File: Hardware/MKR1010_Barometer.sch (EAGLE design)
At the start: 2 parts

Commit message: schematic capture
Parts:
- removed U$1: ARDUINOMICRO, adafruit:ARDUINOMICRO
- added D1: 1N4001, SparkFun-DiscreteSemi:DIODE-PTH
- added J1: (no value), con-jack:JACK-PLUG0
- added J2, J3: 1X2-3.5MM, adafruit:1X2-3.5MM
- added M1: MOTOR10MM, SparkFun-Electromechanical:MOTOR10MM
- added MKR1010: ARDUINOMICRO, adafruit:ARDUINOMICRO
- added T1: TIP122, transistor:TIP122
- R1: value (none) -> 220
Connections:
- new net GND: D1.A, J1.1, J3.1, T1.E
- new net N$2: R1.1, T1.B
- new net N$3: D1.C, M1.-, T1.C
- new net N$4: J1.3, J2.2, M1.+, MKR1010.5V
- new net N$5: J2.1, MKR1010.6
- net N$1: now also MKR1010.7; no longer U$1.NC@2
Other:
- note added: "MKR1010"
- moved on the sheet: R1

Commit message: added terminal to attach MPL115A2
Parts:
- added J4, J5: 1X2-3.5MM, adafruit:1X2-3.5MM
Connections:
- new net N$6: J4.1, MKR1010.SCK
- new net N$7: J4.2, MKR1010.MISO
- net GND: now also J5.2
- net N$4: now also J5.1
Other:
- note added: "Data In Vcc"
- note added: "GND"
- note added: "SCL SDA"
- note added: "To LED Matrix"
- note added: "To MPL115A2 Sensor"
- note added: "Vcc GND"
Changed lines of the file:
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@@
 <part name="SUPPLY2" library="supply2" library_urn="urn:adsk.eagle:library:372" deviceset="GND" device=""/>
 <part name="SUPPLY3" library="supply2" library_urn="urn:adsk.eagle:library:372" deviceset="GND" device=""/>
+<part name="J4" library="adafruit" library_urn="urn:adsk.eagle:library:420" deviceset="1X2" device="-3.5MM" package3d_urn="urn:adsk.eagle:package:6240635/1"/>
+<part name="J5" library="adafruit" library_urn="urn:adsk.eagle:library:420" deviceset="1X2" device="-3.5MM" package3d_urn="urn:adsk.eagle:package:6240635/1"/>
+<part name="SUPPLY4" library="supply2" library_urn="urn:adsk.eagle:library:372" deviceset="GND" device=""/>
 </parts>
 <sheets>
@@
 <plain>
 <text x="0" y="58.42" size="1.778" layer="94" rot="R90">MKR1010</text>
+<text x="43.18" y="45.72" size="1.778" layer="91">To LED Matrix</text>
+<text x="43.18" y="12.7" size="1.778" layer="91">To MPL115A2 Sensor</text>
+<text x="45.72" y="38.1" size="1.778" layer="91">Data In
+Vcc</text>
+<text x="45.72" y="30.48" size="1.778" layer="91">GND</text>
+<text x="45.72" y="5.08" size="1.778" layer="91">SCL
+SDA</text>
+<text x="45.72" y="-5.08" size="1.778" layer="91">Vcc
+GND</text>
 </plain>
 <instances>
@@
 <instance part="SUPPLY3" gate="GND" x="30.48" y="20.32" smashed="yes">
 <attribute name="VALUE" x="28.575" y="17.145" size="1.778" layer="96"/>
+</instance>
+<instance part="J4" gate="G$1" x="38.1" y="5.08" smashed="yes"/>
+<instance part="J5" gate="G$1" x="38.1" y="-5.08" smashed="yes"/>
+<instance part="SUPPLY4" gate="GND" x="30.48" y="-10.16" smashed="yes">
+<attribute name="VALUE" x="28.575" y="-13.335" size="1.778" layer="96"/>
 </instance>
 </instances>
@@
 <wire x1="-22.86" y1="91.44" x2="-22.86" y2="88.9" width="0.1524" layer="91"/>
 </segment>
+<segment>
+<pinref part="J5" gate="G$1" pin="2"/>
+<wire x1="33.02" y1="-5.08" x2="30.48" y2="-5.08" width="0.1524" layer="91"/>
+<pinref part="SUPPLY4" gate="GND" pin="GND"/>
+<wire x1="30.48" y1="-5.08" x2="30.48" y2="-7.62" width="0.1524" layer="91"/>
+</segment>
 </net>
 <net name="N$5" class="0">
@@
 <pinref part="J2" gate="G$1" pin="2"/>
 <wire x1="15.24" y1="38.1" x2="33.02" y2="38.1" width="0.1524" layer="91"/>
+<pinref part="J5" gate="G$1" pin="1"/>
+<wire x1="33.02" y1="-2.54" x2="-17.78" y2="-2.54" width="0.1524" layer="91"/>
+<wire x1="-17.78" y1="-2.54" x2="-17.78" y2="30.48" width="0.1524" layer="91"/>
+<junction x="-17.78" y="30.48"/>
+</segment>
+</net>
+<net name="N$6" class="0">
+<segment>
+<pinref part="MKR1010" gate="G$1" pin="SCK"/>
+<pinref part="J4" gate="G$1" pin="1"/>
+<wire x1="-12.7" y1="38.1" x2="-12.7" y2="7.62" width="0.1524" layer="91"/>
+<wire x1="-12.7" y1="7.62" x2="33.02" y2="7.62" width="0.1524" layer="91"/>
+</segment>
+</net>
+<net name="N$7" class="0">
+<segment>
+<pinref part="MKR1010" gate="G$1" pin="MISO"/>
+<wire x1="-12.7" y1="40.64" x2="-15.24" y2="40.64" width="0.1524" layer="91"/>
+<wire x1="-15.24" y1="40.64" x2="-15.24" y2="5.08" width="0.1524" layer="91"/>
+<pinref part="J4" gate="G$1" pin="2"/>
+<wire x1="-15.24" y1="5.08" x2="33.02" y2="5.08" width="0.1524" layer="91"/>
 </segment>
 </net>
@@
 </drawing>
 <compatibility>
+<note version="6.3" minversion="6.2.2" severity="warning">
+Since Version 6.2.2 text objects can contain more than one line,
+which will not be processed correctly with this version.
+</note>
 <note version="8.2" severity="warning">
 Since Version 8.2, EAGLE supports online libraries. The ids

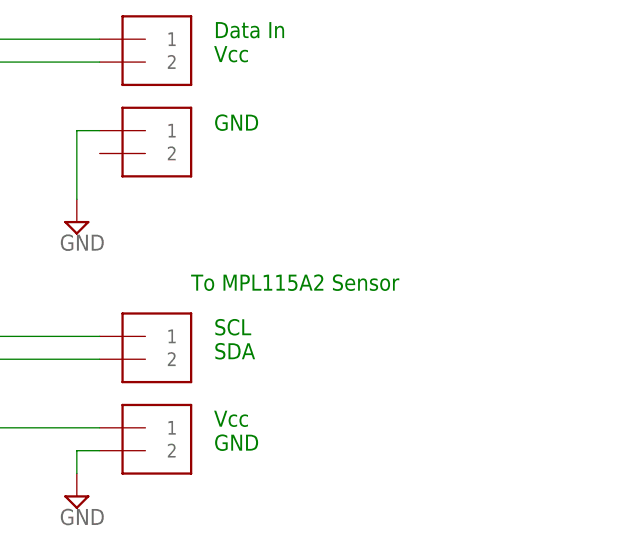
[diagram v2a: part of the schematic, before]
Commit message: Updated schematic with BMP280
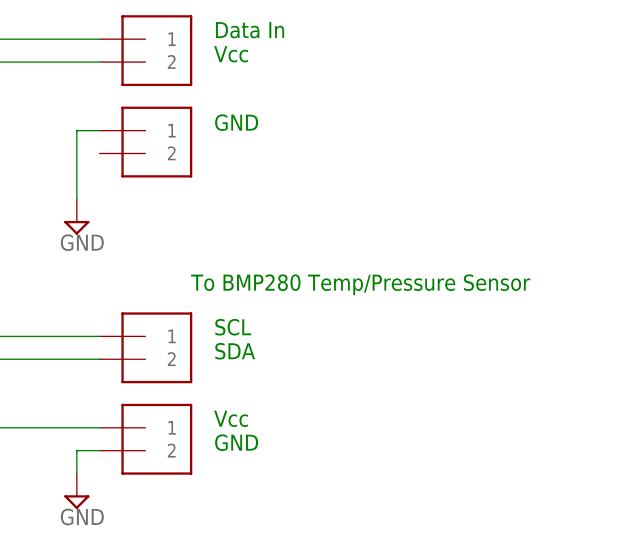
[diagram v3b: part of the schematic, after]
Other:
- note added: "To BMP280 Temp/Pressure Sensor"
- note removed: "To MPL115A2 Sensor"
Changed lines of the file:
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@@
 <grid distance="0.1" unitdist="inch" unit="inch" style="lines" multiple="1" display="no" altdistance="0.01" altunitdist="inch" altunit="inch"/>
 <layers>
-<layer number="1" name="Top" color="4" fill="1" visible="yes" active="no"/>
-<layer number="2" name="Route2" color="16" fill="1" visible="yes" active="no"/>
-<layer number="15" name="Route15" color="23" fill="1" visible="yes" active="no"/>
-<layer number="16" name="Bottom" color="1" fill="1" visible="yes" active="no"/>
-<layer number="17" name="Pads" color="2" fill="1" visible="yes" active="no"/>
-<layer number="18" name="Vias" color="2" fill="1" visible="yes" active="no"/>
-<layer number="19" name="Unrouted" color="6" fill="1" visible="yes" active="no"/>
-<layer number="20" name="Dimension" color="24" fill="1" visible="yes" active="no"/>
-<layer number="21" name="tPlace" color="7" fill="1" visible="yes" active="no"/>
-<layer number="22" name="bPlace" color="7" fill="1" visible="yes" active="no"/>
-<layer number="23" name="tOrigins" color="15" fill="1" visible="yes" active="no"/>
-<layer number="24" name="bOrigins" color="15" fill="1" visible="yes" active="no"/>
-<layer number="25" name="tNames" color="7" fill="1" visible="yes" active="no"/>
-<layer number="26" name="bNames" color="7" fill="1" visible="yes" active="no"/>
-<layer number="27" name="tValues" color="7" fill="1" visible="yes" active="no"/>
-<layer number="28" name="bValues" color="7" fill="1" visible="yes" active="no"/>
+<layer number="1" name="Top" color="4" fill="1" visible="no" active="no"/>
+<layer number="2" name="Route2" color="16" fill="1" visible="no" active="no"/>
+<layer number="15" name="Route15" color="23" fill="1" visible="no" active="no"/>
+<layer number="16" name="Bottom" color="1" fill="1" visible="no" active="no"/>
+<layer number="17" name="Pads" color="2" fill="1" visible="no" active="no"/>
+<layer number="18" name="Vias" color="2" fill="1" visible="no" active="no"/>
+<layer number="19" name="Unrouted" color="6" fill="1" visible="no" active="no"/>
+<layer number="20" name="Dimension" color="24" fill="1" visible="no" active="no"/>
+<layer number="21" name="tPlace" color="7" fill="1" visible="no" active="no"/>
+<layer number="22" name="bPlace" color="7" fill="1" visible="no" active="no"/>
+<layer number="23" name="tOrigins" color="15" fill="1" visible="no" active="no"/>
+<layer number="24" name="bOrigins" color="15" fill="1" visible="no" active="no"/>
+<layer number="25" name="tNames" color="7" fill="1" visible="no" active="no"/>
+<layer number="26" name="bNames" color="7" fill="1" visible="no" active="no"/>
+<layer number="27" name="tValues" color="7" fill="1" visible="no" active="no"/>
+<layer number="28" name="bValues" color="7" fill="1" visible="no" active="no"/>
 <layer number="29" name="tStop" color="7" fill="3" visible="no" active="no"/>
 <layer number="30" name="bStop" color="7" fill="6" visible="no" active="no"/>
@@
 <layer number="35" name="tGlue" color="7" fill="4" visible="no" active="no"/>
 <layer number="36" name="bGlue" color="7" fill="5" visible="no" active="no"/>
-<layer number="37" name="tTest" color="7" fill="1" visible="yes" active="no"/>
-<layer number="38" name="bTest" color="7" fill="1" visible="yes" active="no"/>
+<layer number="37" name="tTest" color="7" fill="1" visible="no" active="no"/>
+<layer number="38" name="bTest" color="7" fill="1" visible="no" active="no"/>
 <layer number="39" name="tKeepout" color="4" fill="11" visible="no" active="no"/>
 <layer number="40" name="bKeepout" color="1" fill="11" visible="no" active="no"/>
@@
 <layer number="44" name="Drills" color="7" fill="1" visible="no" active="no"/>
 <layer number="45" name="Holes" color="7" fill="1" visible="no" active="no"/>
-<layer number="46" name="Milling" color="3" fill="1" visible="yes" active="no"/>
-<layer number="47" name="Measures" color="7" fill="1" visible="yes" active="no"/>
-<layer number="48" name="Document" color="7" fill="1" visible="yes" active="no"/>
-<layer number="49" name="Reference" color="7" fill="1" visible="yes" active="no"/>
-<layer number="50" name="dxf" color="7" fill="1" visible="yes" active="no"/>
-<layer number="51" name="tDocu" color="7" fill="1" visible="yes" active="no"/>
-<layer number="52" name="bDocu" color="7" fill="1" visible="yes" active="no"/>
-<layer number="53" name="tGND_GNDA" color="7" fill="9" visible="yes" active="no"/>
-<layer number="54" name="bGND_GNDA" color="1" fill="9" visible="yes" active="no"/>
-<layer number="56" name="wert" color="7" fill="1" visible="yes" active="no"/>
-<layer number="57" name="tCAD" color="7" fill="1" visible="yes" active="no"/>
-<layer number="59" name="tCarbon" color="7" fill="1" visible="yes" active="no"/>
-<layer number="60" name="bCarbon" color="7" fill="1" visible="yes" active="no"/>
+<layer number="46" name="Milling" color="3" fill="1" visible="no" active="no"/>
+<layer number="47" name="Measures" color="7" fill="1" visible="no" active="no"/>
+<layer number="48" name="Document" color="7" fill="1" visible="no" active="no"/>
+<layer number="49" name="Reference" color="7" fill="1" visible="no" active="no"/>
+<layer number="50" name="dxf" color="7" fill="1" visible="no" active="no"/>
+<layer number="51" name="tDocu" color="7" fill="1" visible="no" active="no"/>
+<layer number="52" name="bDocu" color="7" fill="1" visible="no" active="no"/>
+<layer number="53" name="tGND_GNDA" color="7" fill="9" visible="no" active="no"/>
+<layer number="54" name="bGND_GNDA" color="1" fill="9" visible="no" active="no"/>
+<layer number="56" name="wert" color="7" fill="1" visible="no" active="no"/>
+<layer number="57" name="tCAD" color="7" fill="1" visible="no" active="no"/>
+<layer number="59" name="tCarbon" color="7" fill="1" visible="no" active="no"/>
+<layer number="60" name="bCarbon" color="7" fill="1" visible="no" active="no"/>
 <layer number="88" name="SimResults" color="9" fill="1" visible="yes" active="yes"/>
 <layer number="89" name="SimProbes" color="9" fill="1" visible="yes" active="yes"/>
@@
 <text x="0" y="58.42" size="1.778" layer="94" rot="R90">MKR1010</text>
 <text x="43.18" y="45.72" size="1.778" layer="91">To LED Matrix</text>
-<text x="43.18" y="12.7" size="1.778" layer="91">To MPL115A2 Sensor</text>
+<text x="43.18" y="12.7" size="1.778" layer="91">To BMP280 Temp/Pressure Sensor</text>
 <text x="45.72" y="38.1" size="1.778" layer="91">Data In
 Vcc</text>
